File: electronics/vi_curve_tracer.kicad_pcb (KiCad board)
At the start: 2 copper layers, 60 x 37 mm, 57 parts, among them P1 CONN_01X05, P2 USB_OTG, P3 CONN_01X03, P4 CONN_01X03, U1 MCP6004, U2 pic24f08km202, U3 ft230x

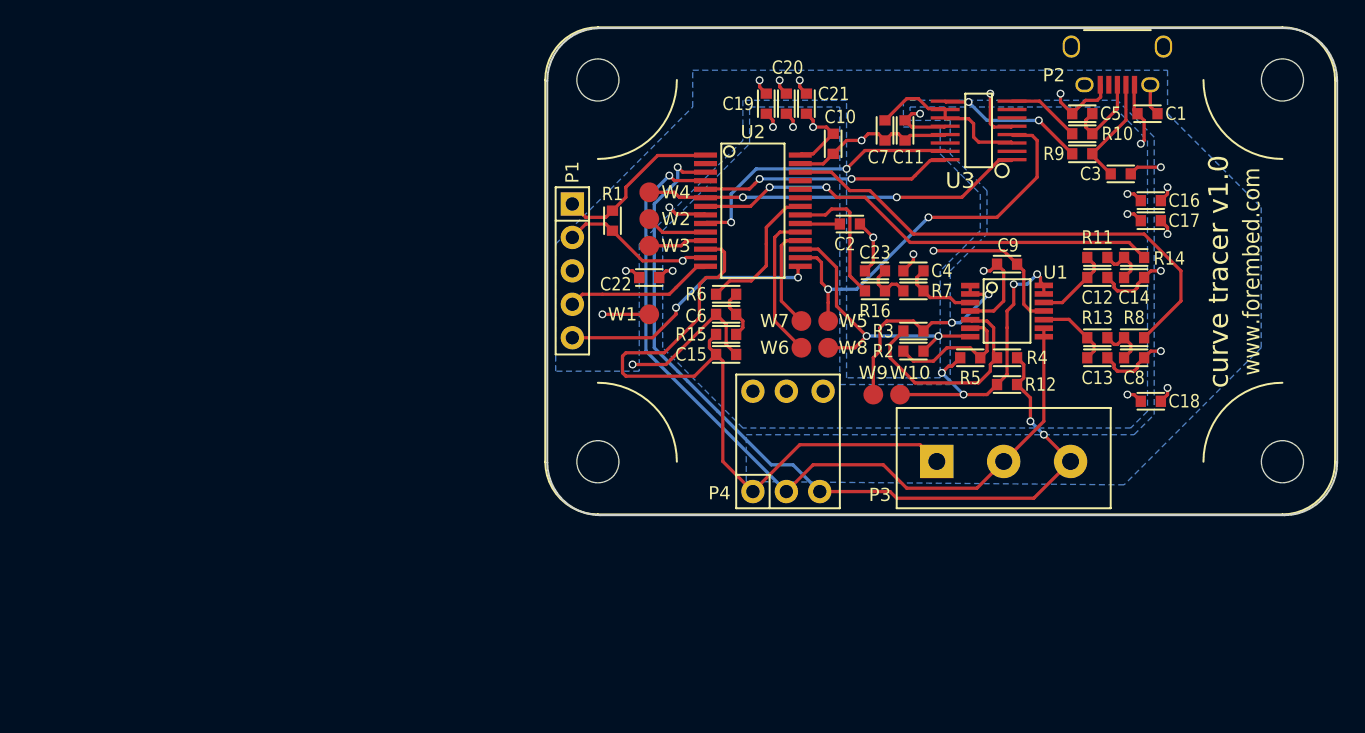
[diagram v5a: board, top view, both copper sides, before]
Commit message: Fixes #8 - Added ground reference on the terminal block
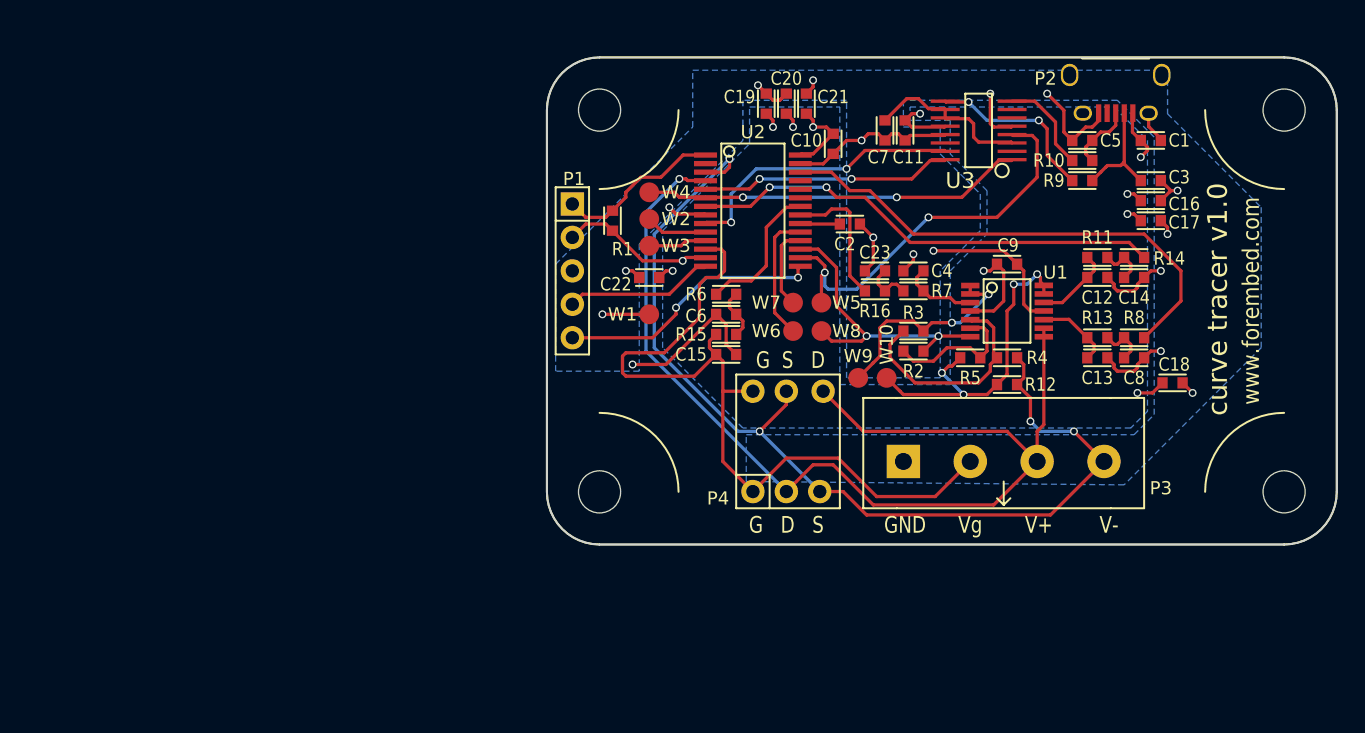
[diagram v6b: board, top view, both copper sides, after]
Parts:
- P3: value CONN_01X03 -> CONN_01X04; footprint kicad_pcb:CONN_1x3_OSTTC032162 -> kicad_pcb:CONN_1x4_OSTTC042162
- P4: value CONN_01X03 -> CONN_01X06
- moved C3 2.34 mm to (212.3, 84.6)
- moved REF** 2.29 mm to (196.5, 93.7)
- moved C18 2.16 mm to (214.0, 99.9)
- moved P2 2.16 mm to (209.7, 75.3)
- moved C1 2.05 mm to (212.3, 81.5)
- moved C5 2.03 mm to (207.1, 81.5)
- moved R10 2.03 mm to (207.1, 83.1)
- moved R9 2.03 mm to (207.1, 84.6)
- moved W9 1.71 mm to (190.1, 99.6)
- moved W10 1.63 mm to (192.3, 99.6)
- moved W7 1.53 mm to (185.2, 93.9)
- moved W5 1.49 mm to (187.3, 93.9)
- moved W6 1.42 mm to (185.2, 96.0)
- moved W8 1.37 mm to (187.3, 96.0)
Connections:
- P3 pad 1: GateVoltage -> GNDD
- P3 pad 2: LD_VOLTAGE_0 -> GateVoltage
- P3 pad 3: LD_VOLTAGE_1 -> LD_VOLTAGE_0
- P4 pad 4: (no net) -> LD_VOLTAGE_0
- P4 pad 5: (no net) -> LD_VOLTAGE_1
- P4 pad 6: (no net) -> GateVoltage
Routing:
- net LD_VOLTAGE_0: track 62.4 -> 82.6 mm
- net LD_VOLTAGE_1: track 64.2 -> 76.9 mm, vias 3 -> 4
- net GateVoltage: track 53.5 -> 59.7 mm
- net Net-(R9-Pad1): track 11.3 -> 13.3 mm
- net Net-(R10-Pad1): track 5.60 -> 7.41 mm
- net Net-(U2-Pad18): track 7.95 -> 6.29 mm
- net /-Vout: track 23.9 -> 25.4 mm
- net Net-(U2-Pad19): track 11.4 -> 9.85 mm
- net Net-(C5-Pad1): track 6.46 -> 5.13 mm
- net GNDD: track 82.4 -> 83.7 mm, vias 19 -> 17
- net /IsenseReference: track 17.3 -> 16.5 mm
- net Net-(R2-Pad1): track 22.3 -> 22.9 mm
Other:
- board text added: "G D S"
- board text added: "G S D"
- board text added: "GND"
- board text added: "V+"
- board text added: "V-"
- board text added: "Vg"

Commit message: See #13 - Added XY outputs to hardware
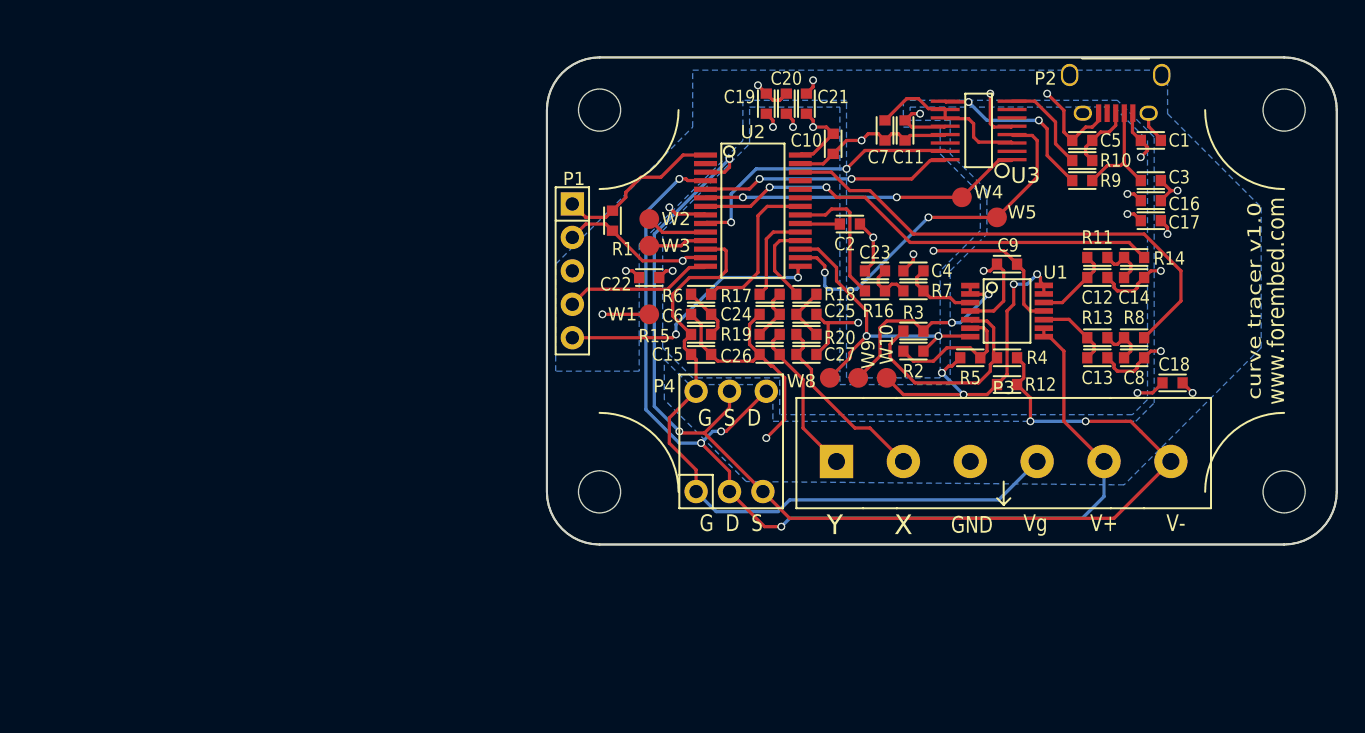
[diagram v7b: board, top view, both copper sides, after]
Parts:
- removed W6, W7: TEST_1P, Measurement_Points:Measurement_Point_Round-SMD-Pad_Small
- added C24: 100nF, kicad_pcb:SM_0603, F.Cu at (183.4, 94.7)
- added C25: 100nF, kicad_pcb:SM_0603, F.Cu at (186.2, 94.7)
- added C26: 100nF, kicad_pcb:SM_0603, F.Cu at (183.4, 97.8)
- added C27: 100nF, kicad_pcb:SM_0603, F.Cu at (186.2, 97.8)
- added R17: 1k, kicad_pcb:SM_0603, F.Cu at (183.4, 93.2)
- added R18: 1k, kicad_pcb:SM_0603, F.Cu at (186.2, 93.2)
- added R19: 1k, kicad_pcb:SM_0603, F.Cu at (183.4, 96.3)
- added R20: 1k, kicad_pcb:SM_0603, F.Cu at (186.2, 96.3)
- P3: value CONN_01X04 -> CONN_01X06; footprint kicad_pcb:CONN_1x4_OSTTC042162 -> kicad_pcb:CONN_1x6_OSTTC062162
- moved W4 23.8 mm to (198.0, 85.9)
- moved W5 14.8 mm to (200.7, 87.4)
- moved P4 4.32 mm to (180.3, 104.4)
- moved W8 3.61 mm to (188.0, 99.6)
- moved C15 1.91 mm to (178.2, 97.8)
- moved C6 1.91 mm to (178.2, 94.7)
- moved R15 1.91 mm to (178.2, 96.3)
- moved R6 1.91 mm to (178.2, 93.2), turned to 0 degrees
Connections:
- P3 pad 1: GNDD -> /y
- P3 pad 2: GateVoltage -> /x
- P3 pad 3: LD_VOLTAGE_0 -> GNDD
- P3 pad 4: LD_VOLTAGE_1 -> GateVoltage
- U2 pad 18: Net-(U2-Pad18) -> PWM3
- U2 pad 19: Net-(U2-Pad19) -> PWM4
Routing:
- net /x: track 0.00 -> 14.1 mm
- net GNDD: track 83.7 -> 97.5 mm, vias 17 -> 18
- net LD_VOLTAGE_1: track 76.9 -> 89.9 mm
- net /y: track 0.00 -> 11.9 mm
- net Net-(U2-Pad19): track 9.85 -> 0.00 mm
- net PWM4: track 0.00 -> 7.24 mm
- net PWM3: track 0.00 -> 6.49 mm
- net Net-(U2-Pad18): track 6.29 -> 0.00 mm
- net GateVoltage: track 59.7 -> 53.9 mm
- net FT230X_TX: track 28.9 -> 24.5 mm
- net Net-(C25-Pad1): track 0.00 -> 4.31 mm
- net Net-(C24-Pad1): track 0.00 -> 4.10 mm
- net FT230X_RX: track 30.7 -> 28.3 mm
- net /PWM2: track 10.9 -> 12.2 mm
- net LD_VOLTAGE_0: track 82.6 -> 82.5 mm, vias 1 -> 4
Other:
- board text added: "X"
- board text added: "Y"

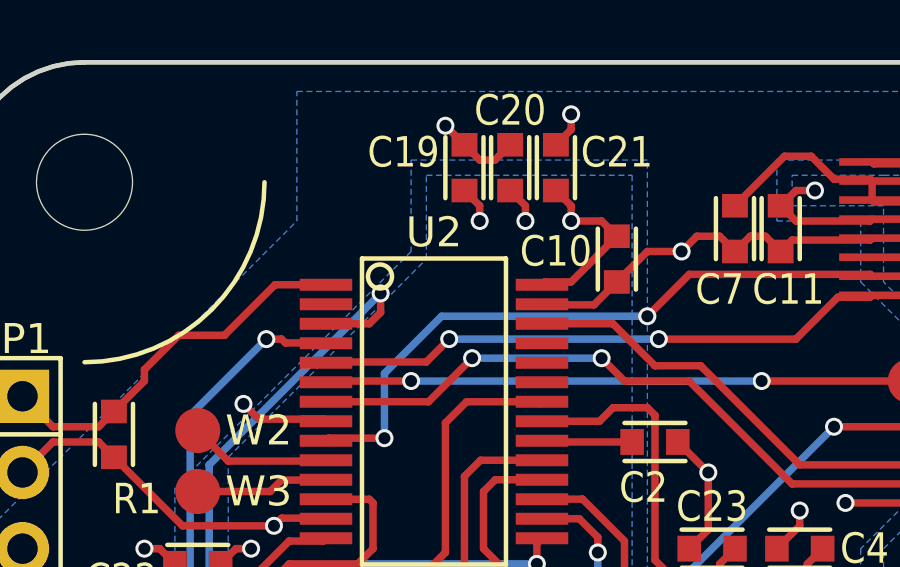
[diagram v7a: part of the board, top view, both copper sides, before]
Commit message: Added extra header to short in case we want to add a bootloader later
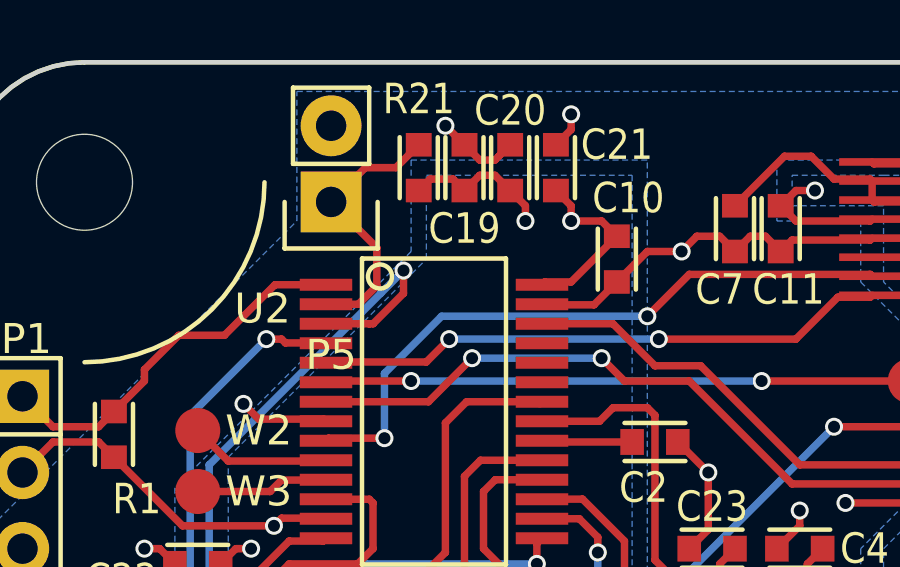
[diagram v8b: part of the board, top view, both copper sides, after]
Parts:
- added P5: CONN_01X02, Pin_Headers:Pin_Header_Straight_1x02, F.Cu at (178.7, 79.9)
- added R21: 10k, kicad_pcb:SM_0603, F.Cu at (181.6, 78.7)
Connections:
- U2 pad 2: (no net) -> ~BOOT
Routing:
- net ~BOOT: track 0.00 -> 9.09 mm
- net +5V: track 42.1 -> 44.6 mm, vias 11 -> 10
- net LD_VOLTAGE_1: track 89.9 -> 92.1 mm
